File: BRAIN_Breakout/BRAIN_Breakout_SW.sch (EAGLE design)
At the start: 80 parts

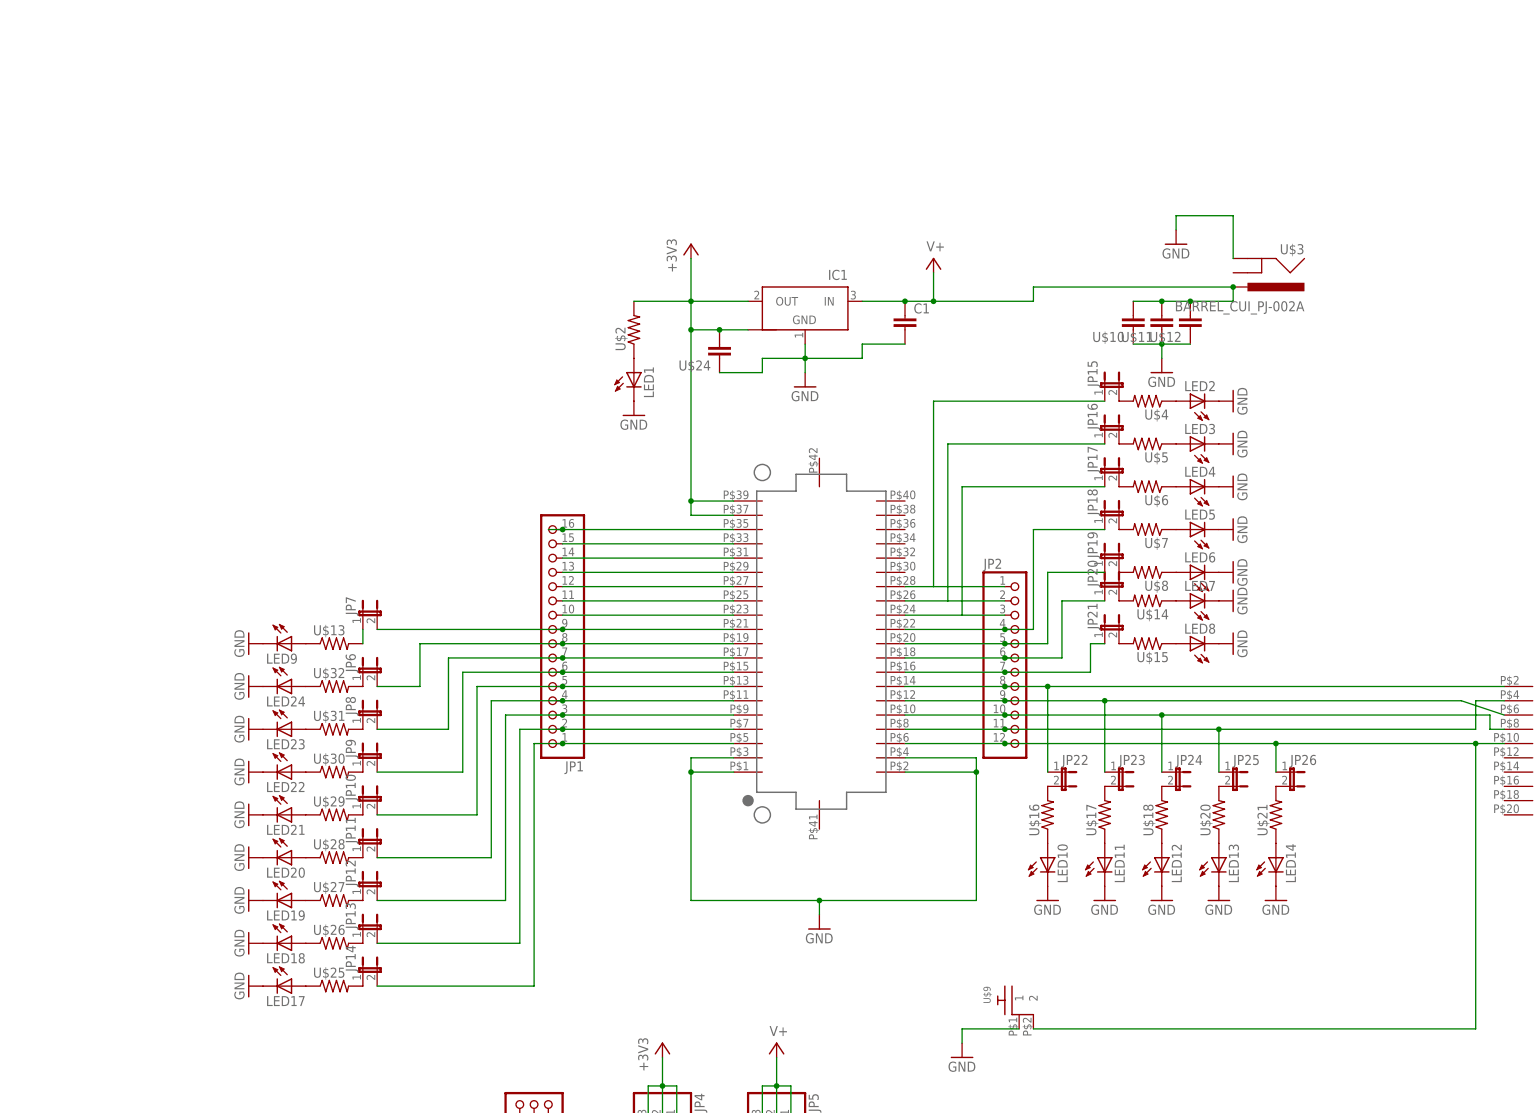
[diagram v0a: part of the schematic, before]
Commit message: Commit board w/switches & fixes (updated to v1.1)
Hadn't previousy committed produced board (includes Gerbers). Just fixed
JTAG and RESET button ground traces and incremented date + version to
1.1 and 7/16
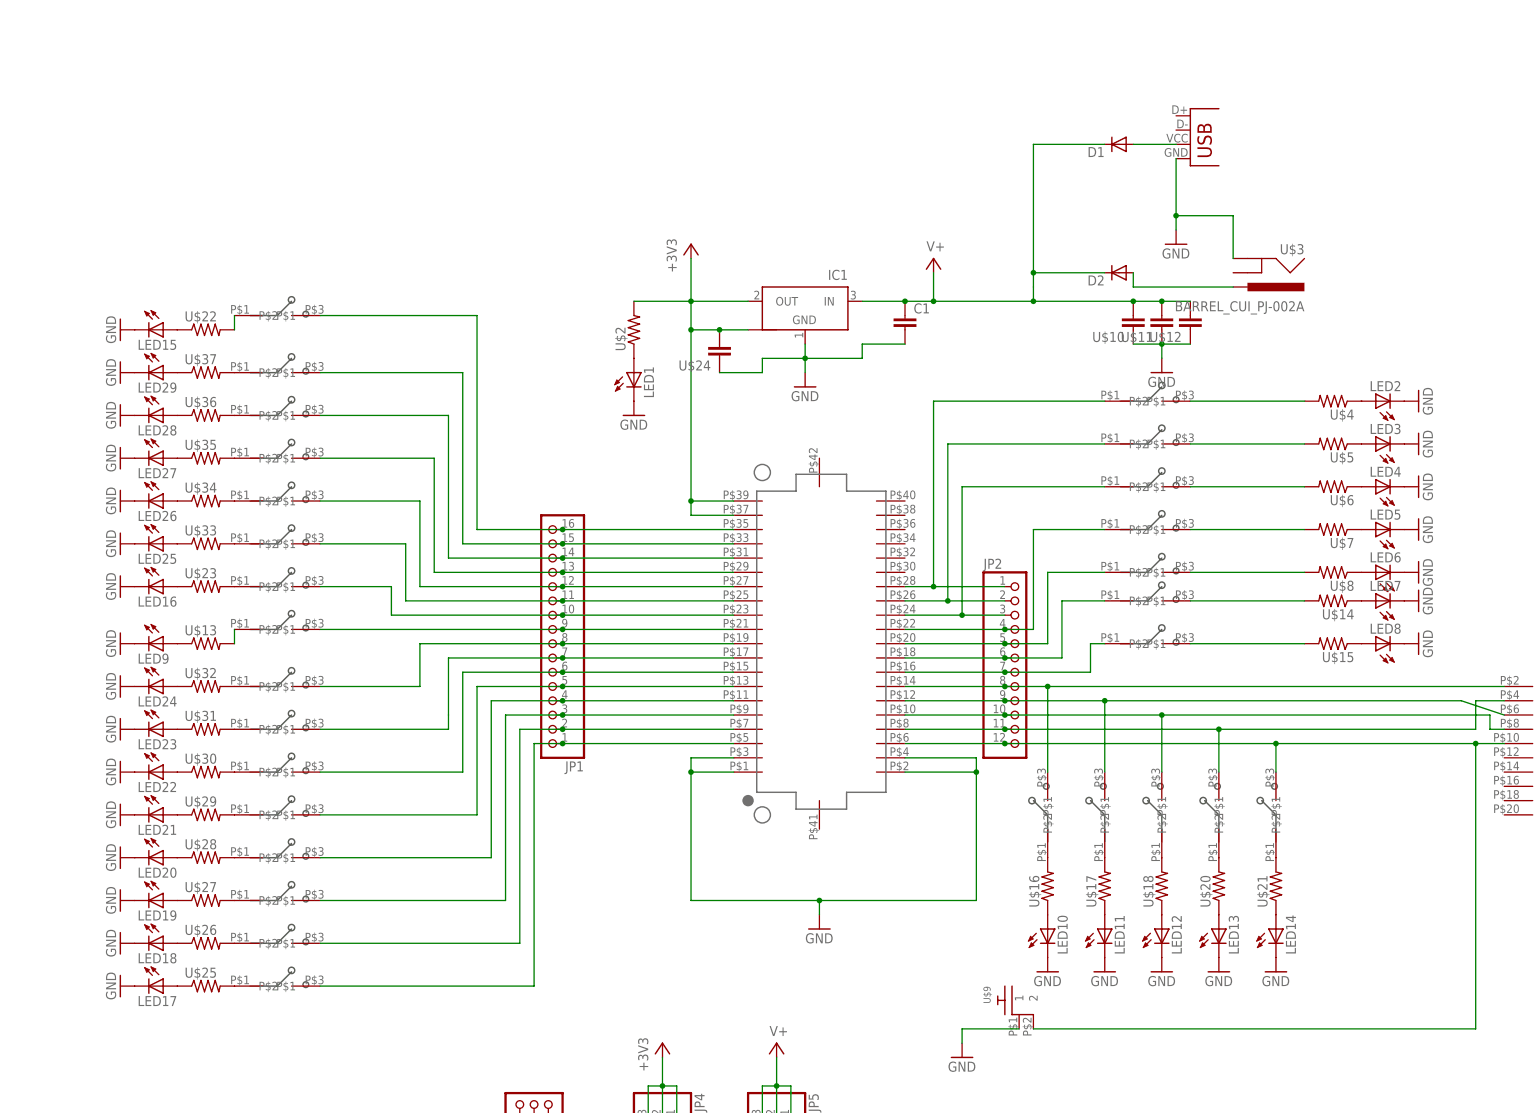
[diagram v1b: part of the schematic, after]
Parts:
- removed JP10, JP11, JP12, JP13, JP14, JP15, JP16, JP17, JP18, JP19, JP20, JP21, JP22, JP23, JP24, JP25, JP26, JP6, JP7, JP8, JP9: (no value), SparkFun:JUMPER-2SMD-NO-NS
- added D1, D2: (no value), SparkFun:DIODESMA
- added LED15, LED16, LED25, LED26, LED27, LED28, LED29: (no value), adafruit:LEDCHIP-LED0805
- added U$22, U$23, U$33, U$34, U$35, U$36, U$37: (no value), GW-devices:RF-R0805
- added U$38, U$39, U$40, U$41, U$42, U$43, U$44, U$45, U$46, U$47, U$48, U$49, U$50, U$51, U$52, U$53, U$54, U$55, U$56, U$57, U$58, U$59, U$60, U$61, U$62, U$63, U$64, U$65: CJS, KW2:CJS
- added X1: USB, SparkFun:USB
- C1, U$12, U$24: MFGN (none) -> Murata; MFGP (none) -> GRM219R61E106KA12D
- JP1: MFGN (none) -> Sullins Connector; MFGP (none) -> PRPC016SAAN-RC
- JP2: MFGN (none) -> Sullins Connector; MFGP (none) -> PRPC012SAAN-RC
- JP3, JP4, JP5: MFGN (none) -> Sullins Connector; MFGP (none) -> PRPC003SAAN-RC
- LED1: MFGN (none) -> Wurth Electronics Inc; MFGP (none) -> 150080BS75000
- U$1: MFGN (none) -> Hirose; MFGP (none) -> DF12(3.0)-40DP-0.5V(86)
- U$10: MFGN (none) -> TDK; MFGP (none) -> C2012X5R1H104K085AA
- U$11: MFGN (none) -> TDK; MFGP (none) -> C2012X5R1E105K125AA
- U$13, U$14, U$15, U$16, U$17, U$18, U$20, U$21, U$25, U$26, U$27, U$28, U$29, U$30, U$31, U$32, U$4, U$5, U$6, U$7, U$8: MFGN (none) -> Panasonic; MFGP (none) -> ERJ-6ENF2001V
- U$19: MFGN (none) -> CNC Tech; MFGP (none) -> 3220-20-0100-00
- U$2: MFGN (none) -> Panasonic; MFGP (none) -> ERJ-6ENF2000V
- U$3: MFGN (none) -> CUI; MFGP (none) -> PJ002-A
- U$9: MFGN (none) -> TE; MFGP (none) -> 1825027-5
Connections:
- new net N$28: LED15.A, U$22.1
- new net N$33: LED16.A, U$23.1
- new net N$34: LED25.A, U$33.1
- new net N$35: LED26.A, U$34.1
- new net N$36: LED27.A, U$35.1
- new net N$46: LED28.A, U$36.1
- new net N$63: LED29.A, U$37.1
- new net N$64: U$22.2, U$45.P$1
- new net N$65: U$35.2, U$48.P$1
- new net N$66: U$34.2, U$49.P$1
- new net N$67: U$33.2, U$50.P$1
- new net N$68: U$23.2, U$51.P$1
- new net N$69: U$32.2, U$52.P$1
- new net N$70: U$30.2, U$53.P$1
- new net N$71: D2.A, U$3.PWR
- new net N$72: D1.A, X1.VBUS
- net GND: now also LED15.C, LED16.C, LED25.C, LED26.C, LED27.C, LED28.C, LED29.C, X1.GND
- net N$10: now also U$44.P$1; no longer JP7.1
- net N$11: now also U$65.P$2; no longer JP21.2
- net N$12: now also U$64.P$2; no longer JP20.2
- net N$13: now also U$63.P$2; no longer JP19.2
- net N$14: now also U$62.P$2; no longer JP18.2
- net N$15: now also U$61.P$2; no longer JP17.2
- net N$16: now also U$60.P$2; no longer JP16.2
- net N$17: now also U$59.P$2; no longer JP15.2
- net N$18: now also U$25.2, U$38.P$1; no longer JP6.1, U$32.2
- net N$19: now also U$26.2, U$39.P$1; no longer JP8.1, U$31.2
- net N$20: now also U$27.2, U$40.P$1; no longer JP9.1, U$30.2
- net N$21: now also U$59.P$1; no longer JP15.1
- net N$22: now also U$60.P$1; no longer JP16.1
- net N$23: now also U$61.P$1; no longer JP17.1
- net N$24: now also U$62.P$1; no longer JP18.1
- net N$25: now also U$63.P$1; no longer JP19.1
- net N$26: now also U$64.P$1; no longer JP20.1
- net N$27: now also U$65.P$1; no longer JP21.1
- net N$41: now also U$28.2, U$41.P$1; no longer JP10.1, U$29.2
- net N$42: now also U$29.2, U$42.P$1; no longer JP11.1, U$28.2
- net N$43: now also U$31.2, U$43.P$1; no longer JP14.1, U$25.2
- net N$44: now also U$37.2, U$46.P$1; no longer JP13.1, U$26.2
- net N$45: now also U$36.2, U$47.P$1; no longer JP12.1, U$27.2
- net N$48: now also U$54.P$2; no longer JP22.1
- net N$50: now also U$54.P$1; no longer JP22.2
- net N$51: now also U$55.P$2; no longer JP23.1
- net N$53: now also U$55.P$1; no longer JP23.2
- net N$54: now also U$56.P$2; no longer JP24.1
- net N$56: now also U$56.P$1; no longer JP24.2
- net N$57: now also U$57.P$2; no longer JP25.1
- net N$59: now also U$57.P$1; no longer JP25.2
- net N$60: now also U$58.P$2; no longer JP26.1
- net N$62: now also U$58.P$1; no longer JP26.2
- net PTD1: now also U$38.P$2; no longer JP14.2
- net PTD2: now also U$39.P$2; no longer JP13.2
- net PTD3: now also U$40.P$2; no longer JP12.2
- net PTD4: now also U$41.P$2; no longer JP11.2
- net PTD5: now also U$42.P$2; no longer JP10.2
- net PTD6: now also U$53.P$2; no longer JP9.2
- net PTD7: now also U$43.P$2; no longer JP8.2
- net PTE0: now also U$52.P$2; no longer JP6.2
- net PTE1: now also U$44.P$2; no longer JP7.2
- net PTE16: now also U$48.P$2
- net PTE17: now also U$47.P$2
- net PTE18: now also U$46.P$2
- net PTE19: now also U$45.P$2
- net PTE2: now also U$51.P$2
- net PTE3: now also U$50.P$2
- net PTE4: now also U$49.P$2
- net V+: now also D1.C, D2.C; no longer U$3.PWR
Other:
- moved on the sheet: LED10, LED11, LED12, LED13, LED14, LED17, LED18, LED19, LED2, LED20, LED21, LED22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
